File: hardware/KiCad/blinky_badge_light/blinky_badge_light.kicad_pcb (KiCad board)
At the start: 4 copper layers, 135.8 x 109.7 mm, 99 parts, among them Q2 Q_PMOS_GSD, SW1 TS-1187A-B-A-B, U1 ESP32-S3-WROOM-1, U2 TP4056, U3 AP2112K-3.3, U4 MT3608, U5 CP2102N-Axx-xQFN24, U6 SN74LVC1T45DBV

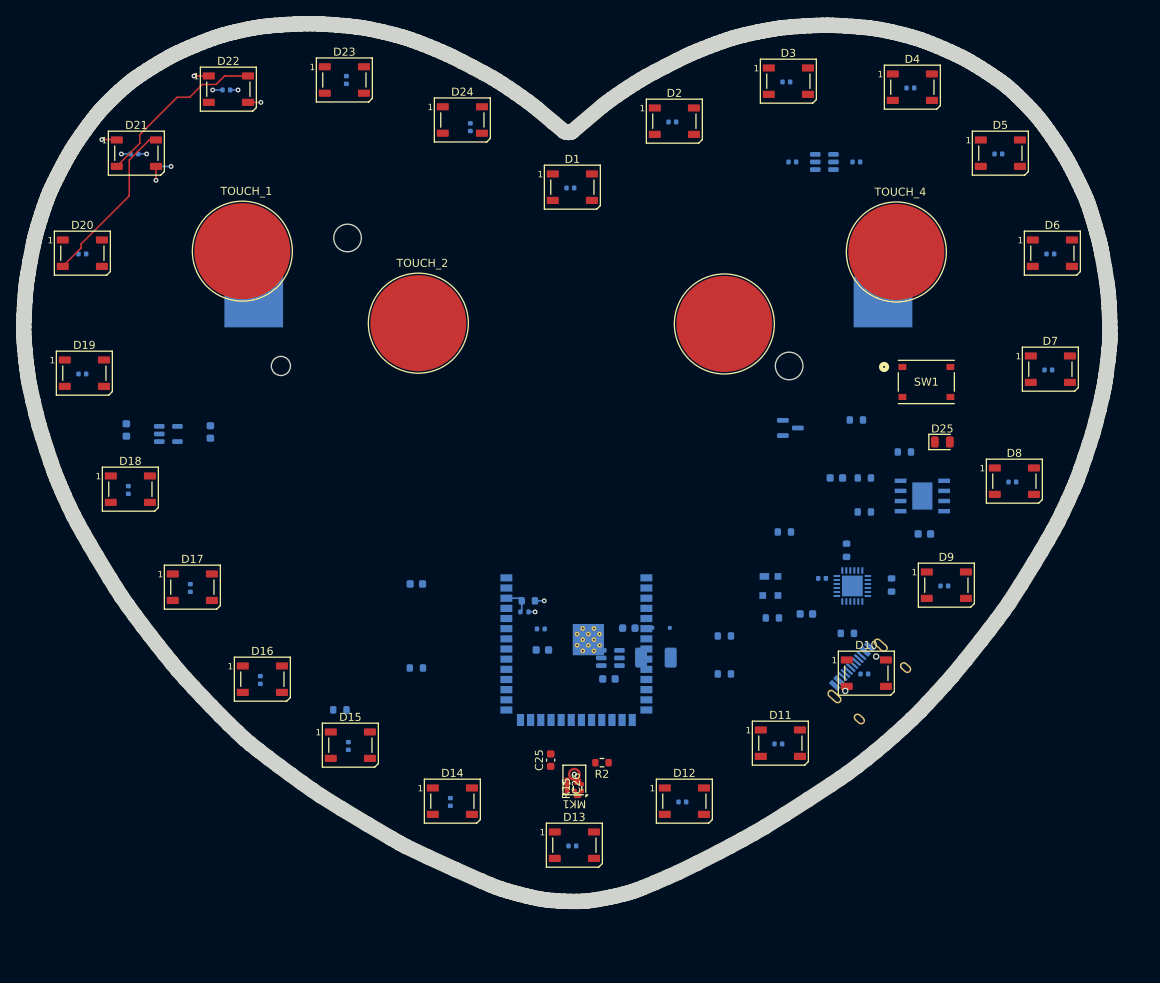
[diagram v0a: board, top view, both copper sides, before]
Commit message: changing led locations
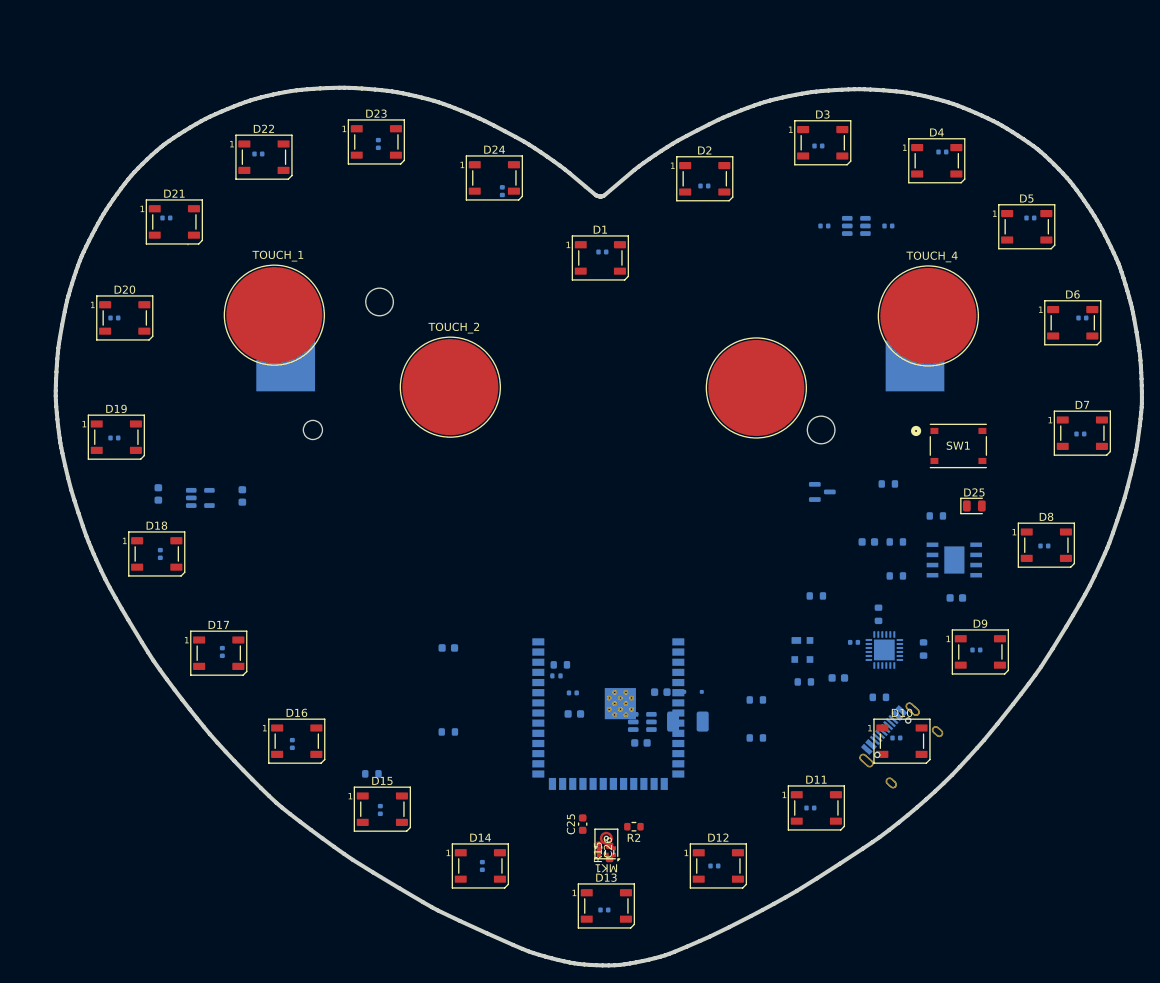
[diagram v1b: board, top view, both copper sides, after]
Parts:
- moved D21 9.82 mm to (96.8, 61.8)
- moved D5 9.77 mm to (203.3, 62.4)
- moved D4 9.69 mm to (192.1, 54.1)
- moved D20 9.68 mm to (90.5, 73.8)
- moved D22 9.59 mm to (108.0, 53.6)
- moved D10 9.59 mm to (187.7, 126.7)
- moved D1 9.52 mm to (150.0, 66.2)
- moved D9 9.37 mm to (197.5, 115.5)
- moved D11 9.27 mm to (177.0, 135.0)
- moved D12 9.15 mm to (164.8, 142.2)
- moved D6 9.07 mm to (209.1, 74.3)
- moved R12 8.94 mm to (121.4, 130.7)
- moved BT1 8.94 mm to (150.0, 79.8)
- moved C1 8.94 mm to (150.2, 65.5)
- moved C10 8.94 mm to (187.0, 126.2)
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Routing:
- net Net-(D21-DOUT): track 21.7 -> 0.00 mm
- net Net-(D20-DOUT): track 21.1 -> 0.00 mm
- net 5V Power: track 9.86 -> 0.00 mm, vias 6 -> 0
- net GND: track 4.62 -> 0.04 mm, vias 4 -> 0
- net ESP32 Reset: track 4.01 -> 0.00 mm
- net 3.3V Power: track 1.19 -> 0.00 mm, vias 1 -> 0
- removed copper zone on In2.Cu, net 3.3V Power
- removed copper zone on In2.Cu, net 5V Power
- removed copper zone on In1.Cu, net GND

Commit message: placing items on the board
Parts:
- added REF**: MountingHole_3mm, MountingHole:MountingHole_3mm, F.Cu at (122.0, 65.0)
- added REF**: MountingHole_3mm, MountingHole:MountingHole_3mm, F.Cu at (178.0, 65.0)
- added REF**: MountingHole_3mm, MountingHole:MountingHole_3mm, F.Cu at (150.0, 128.0)
- C25, C26, MK1, R15, R2: moved to B.Cu
- C31: footprint Resistor_SMD:R_0402_1005Metric -> Capacitor_SMD:C_0402_1005Metric
- TOUCH_4: footprint footprints:TestPoint_Pad_D12.0mm -> TestPoint:TestPoint_Pad_D4.0mm
- moved C33 81.9 mm to (112.9, 101.4)
- moved D25 78.3 mm to (118.9, 89.0)
- moved U2 74.9 mm to (119.5, 98.7)
- moved R9 74.4 mm to (112.5, 106.3)
- moved R4 74.4 mm to (112.9, 99.4), turned to 180 degrees
- moved R3 74.3 mm to (112.9, 95.7)
- moved R14 73.3 mm to (118.9, 93.4)
- moved SW1 72.9 mm to (123.6, 105.8)
- moved C32 70.7 mm to (112.9, 97.5), turned to 180 degrees
- moved C37 69.9 mm to (127.7, 100.7), turned to 90 degrees
- moved U6 65.2 mm to (130.2, 101.8), turned to -90 degrees
- moved C36 64.8 mm to (127.7, 103.0), turned to -90 degrees
- moved Q2 61.6 mm to (117.0, 105.8)
- moved TOUCH_4 56.2 mm to (162.4, 121.9)
- moved R15 38.3 mm to (134.2, 106.2), turned to 0 degrees
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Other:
- board size 135.8 x 109.7 mm -> 108.6 x 87.8 mm

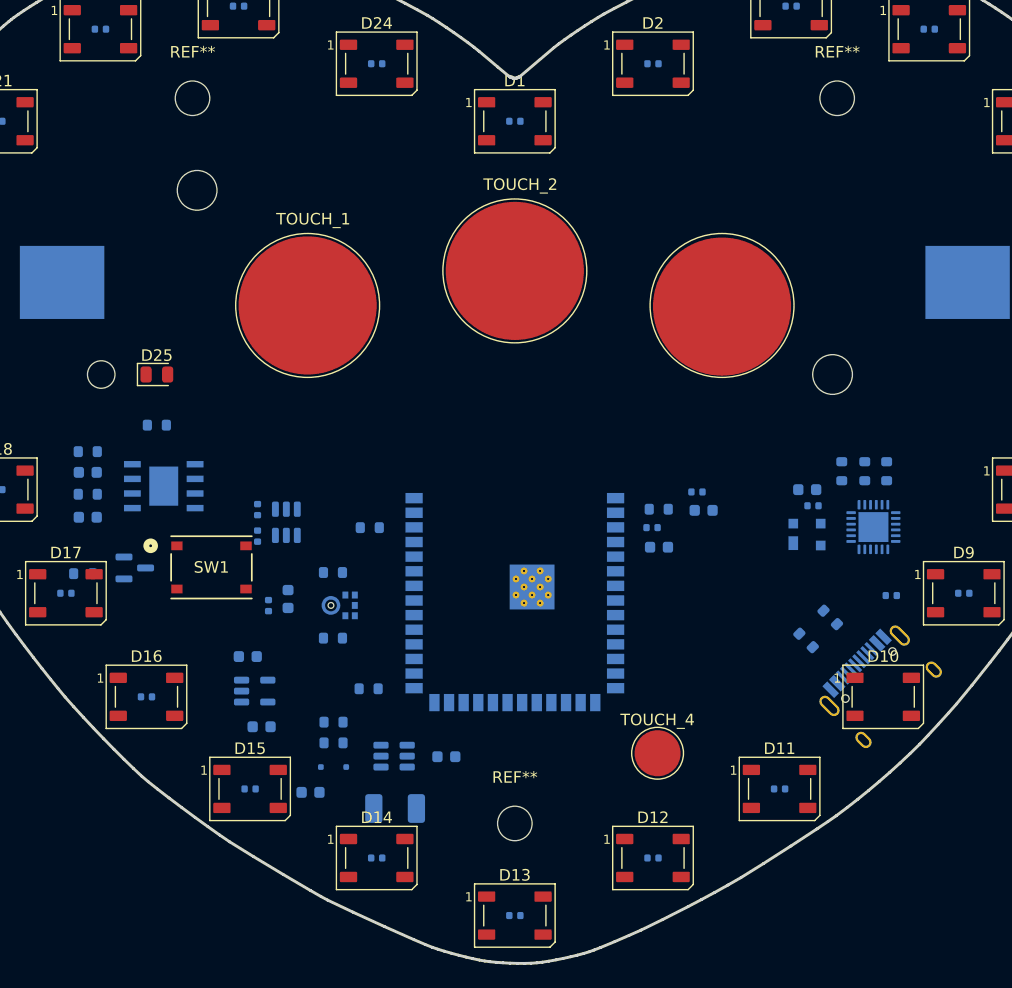
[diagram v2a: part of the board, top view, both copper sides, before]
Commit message: fix some stuff with the footprints, rearrange some things
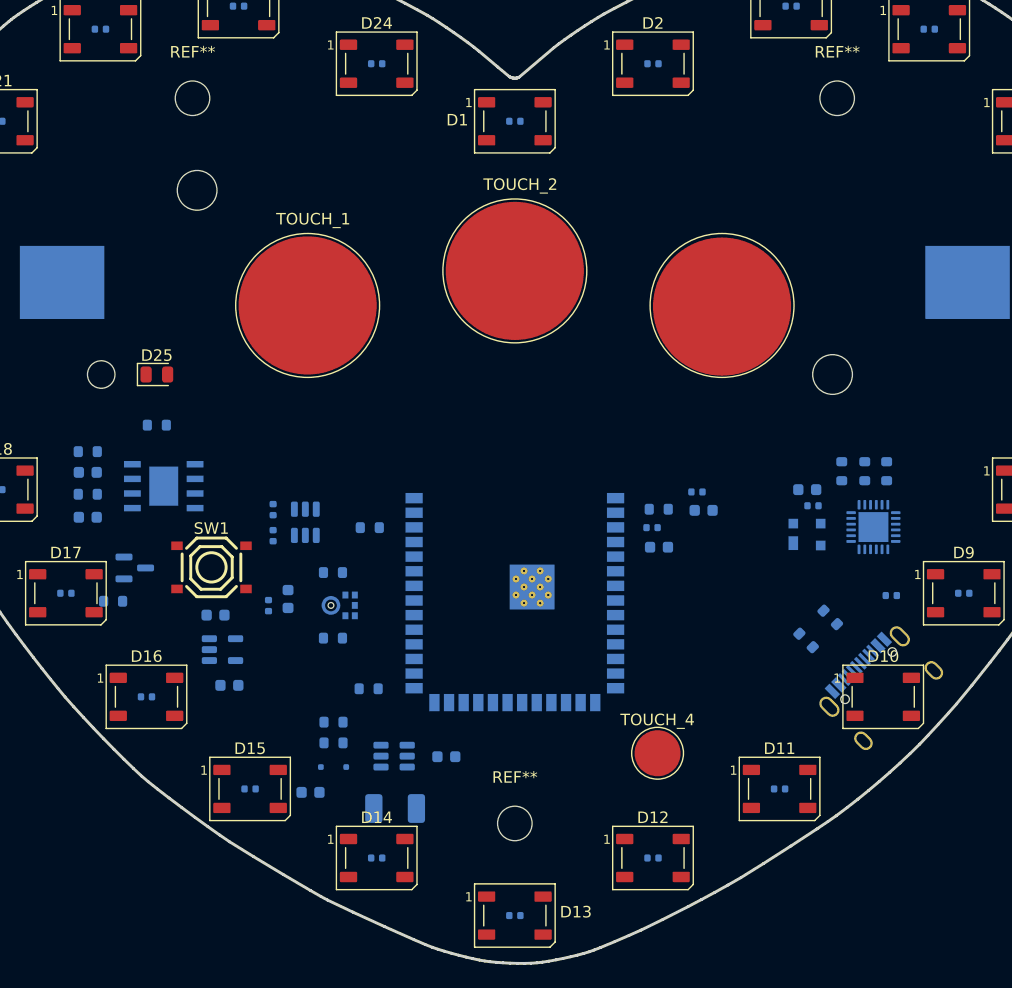
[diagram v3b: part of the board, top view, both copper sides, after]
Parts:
- SW1: footprint footprints:TS-1187A-B-A-B_XKB -> footprints:SW-SMD_4P-L5.1-W5.1-P3.70-LS6.5-TL_H1.5
- USBC1: footprint Connector_USB:USB_C_Receptacle_HRO_TYPE-C-31-M-12 -> footprints:USB-C_SMD-TYPE-C-31-M-12
- moved U3 4.56 mm to (124.6, 112.9)
- moved C34 4.56 mm to (124.0, 109.9)
- moved C35 4.56 mm to (125.2, 116.0)
- moved R9 3.54 mm to (115.1, 108.7)
- moved U6 1.65 mm to (131.8, 101.8)
- moved USBC1 1.38 mm to (181.6, 116.0)
- moved C36 1.35 mm to (129.0, 103.0)
- moved C37 1.35 mm to (129.0, 100.7)
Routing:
- added copper zone on In2.Cu, net 3.3V Power
- added copper zone on In2.Cu, net 5V Power

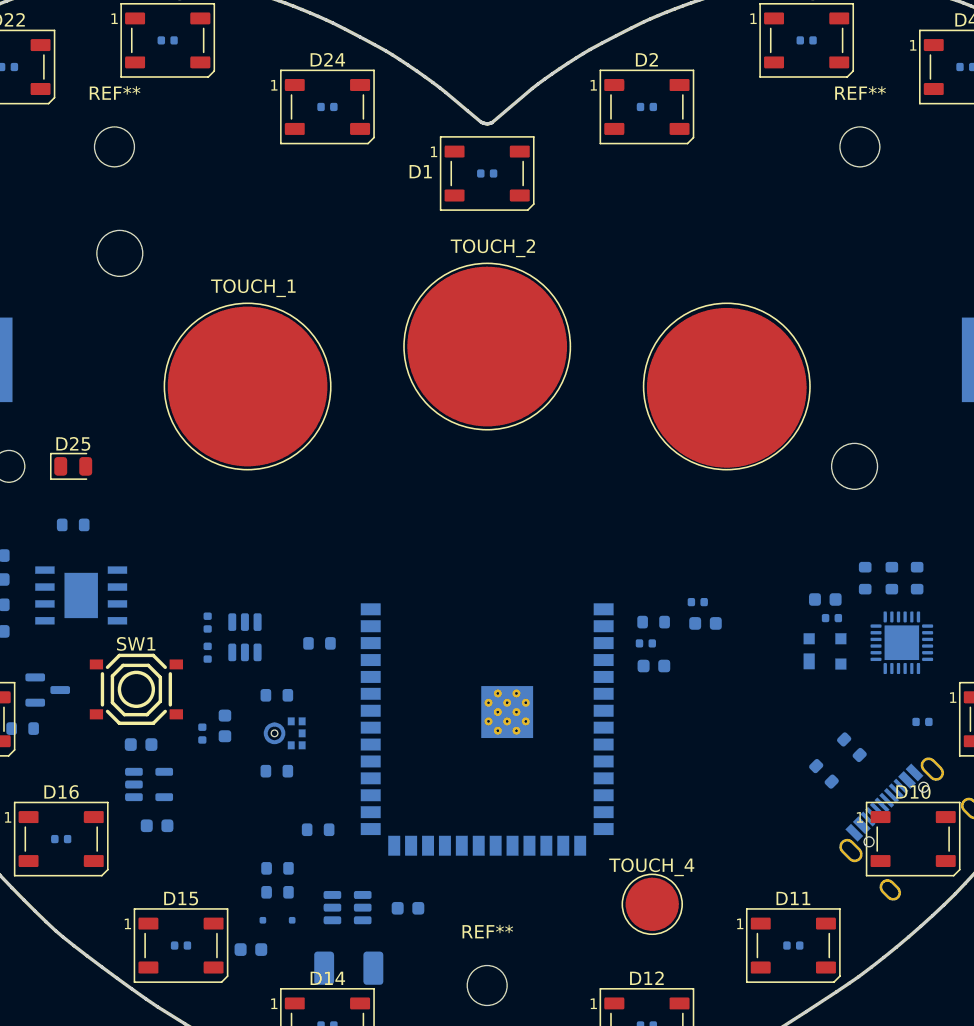
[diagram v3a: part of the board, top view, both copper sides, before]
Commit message: pad 4 is now stop sign shaped since its the off button
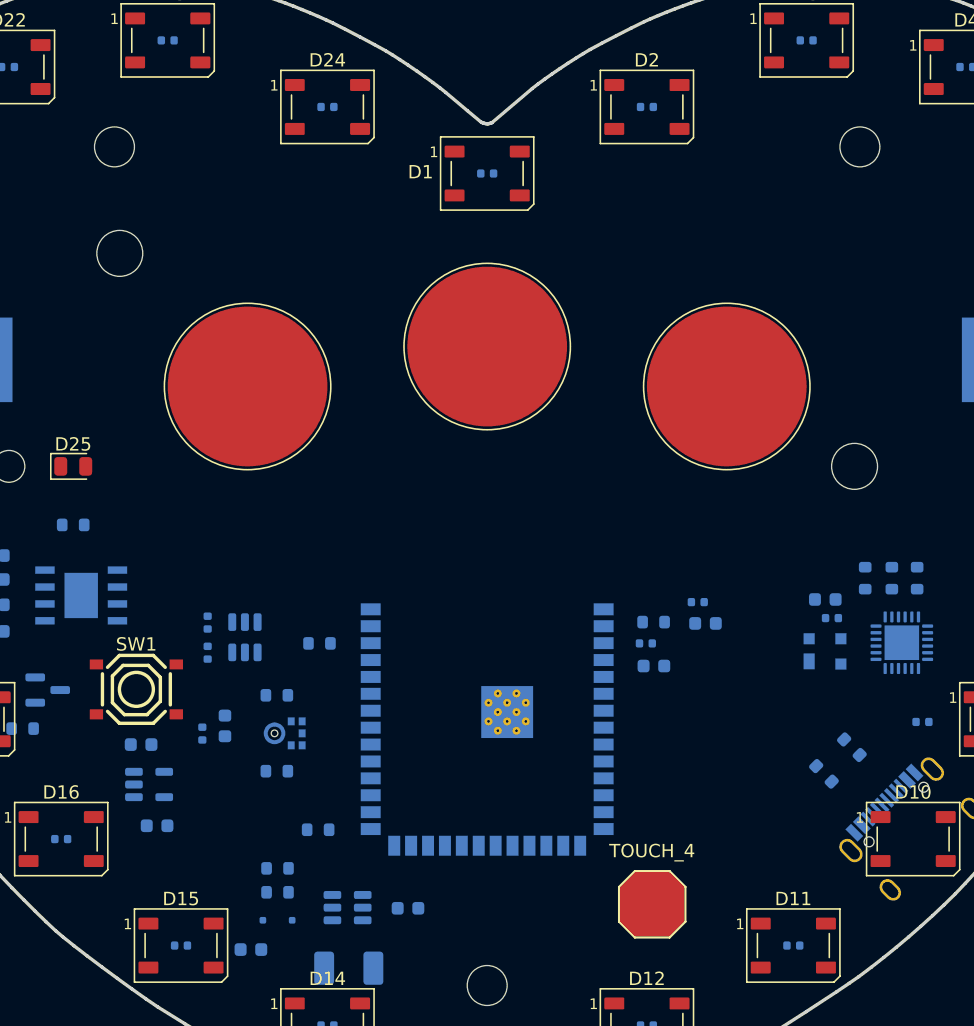
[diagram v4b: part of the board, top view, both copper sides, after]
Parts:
- TOUCH_4: footprint TestPoint:TestPoint_Pad_D4.0mm -> footprints:Touch_Pad_StopSign_6mm

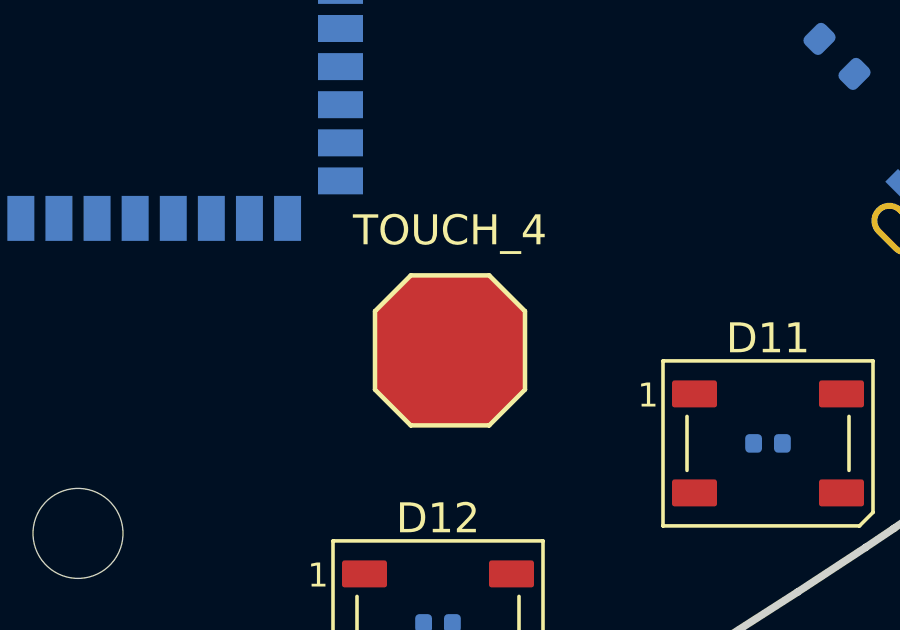
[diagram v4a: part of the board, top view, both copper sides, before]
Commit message: add exclusion zone for pads/screw holes for fill area
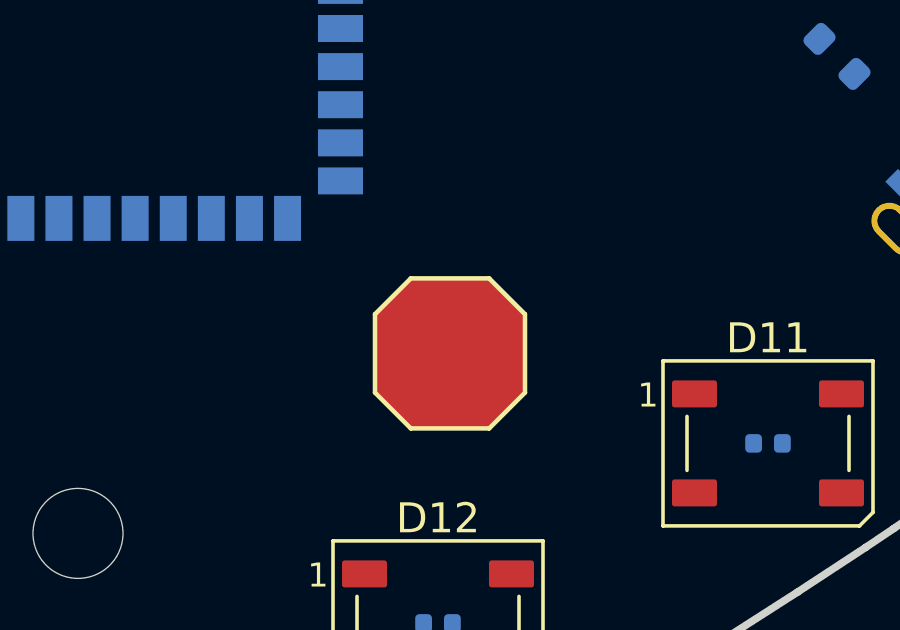
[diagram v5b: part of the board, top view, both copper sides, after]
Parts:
- U1: value ESP32-S3-WROOM-1 -> ESP32-S3-WROOM-1 - no antenna keep out; footprint RF_Module:ESP32-S3-WROOM-1 -> footprints:ESP32-S3-WROOM-1 - no antenna keep out
- moved TOUCH_4 0.10 mm to (162.4, 122.0)
